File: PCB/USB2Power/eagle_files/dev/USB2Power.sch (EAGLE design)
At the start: 7 parts, among them SW1 PCM12SMTR

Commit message: All connected up. Also added ground for the other two header pins as opposed to NC. Made connections a little better. Some known DRC failures.
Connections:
- net GND: now also JP1.3, JP1.4
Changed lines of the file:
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@@
 <label x="73.66" y="22.86" size="1.778" layer="95"/>
+</segment>
+<segment>
+<pinref part="JP1" gate="G$1" pin="4"/>
+<wire x1="63.5" y1="33.02" x2="76.2" y2="33.02" width="0.1524" layer="91"/>
+<label x="71.12" y="33.02" size="1.778" layer="95"/>
+</segment>
+<segment>
+<pinref part="JP1" gate="G$1" pin="3"/>
+<wire x1="63.5" y1="30.48" x2="76.2" y2="30.48" width="0.1524" layer="91"/>
+<label x="71.12" y="30.48" size="1.778" layer="95"/>
 </segment>
 </net>

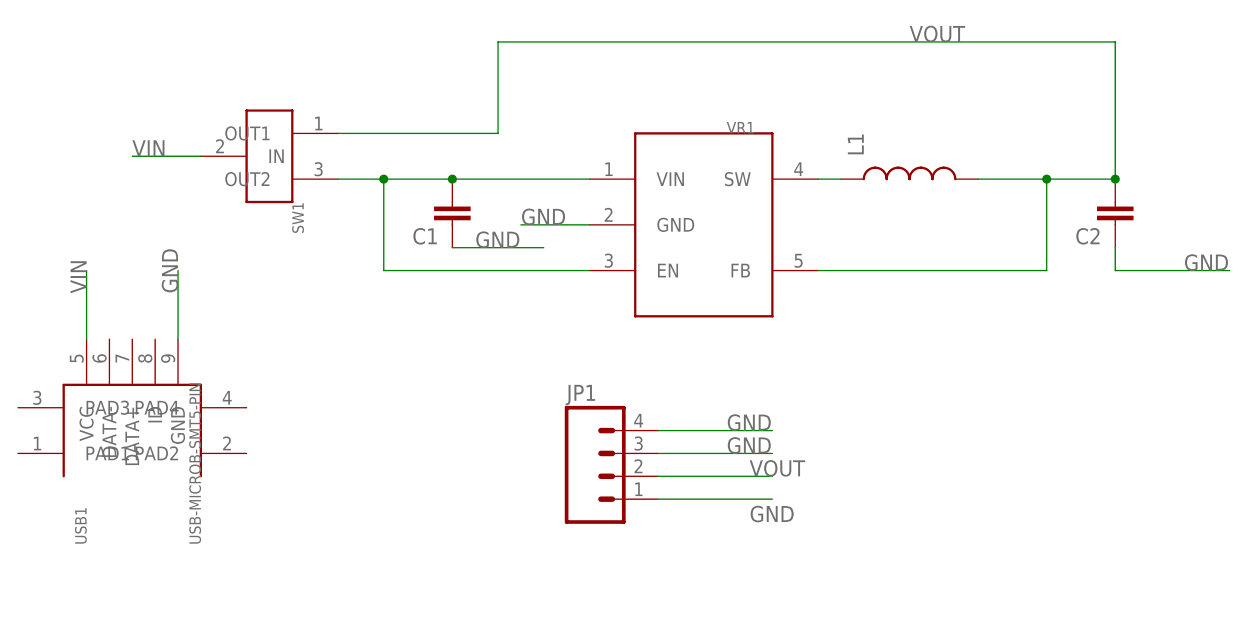
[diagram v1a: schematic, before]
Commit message: Add separate headers for 5V and 3V power outputs. Joint header + inductor may have been causing problems.
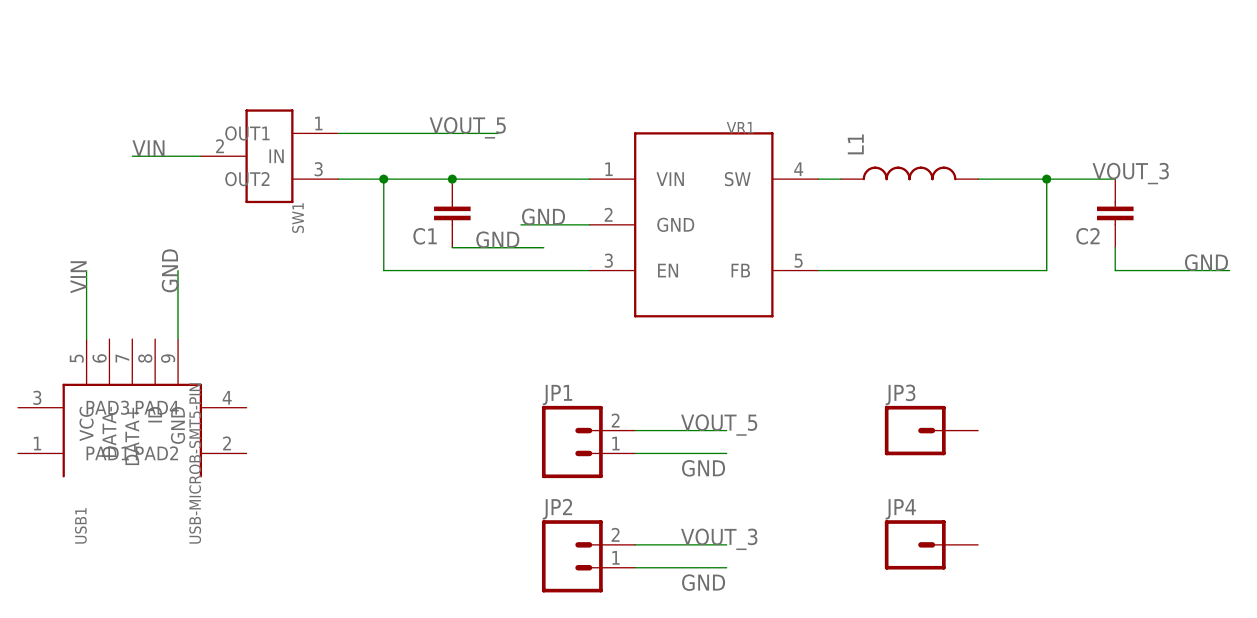
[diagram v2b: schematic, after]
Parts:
- added JP2: (no value), SparkFun-Connectors:M02PTH
- added JP3, JP4: (no value), SparkFun-Connectors:M01PTH
- JP1: device SparkFun-Connectors:M04PTH -> SparkFun-Connectors:M02PTH
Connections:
- removed net VOUT: C2.2, JP1.2, L1.2, SW1.OUT1, VR1.FB
- new net VOUT_3: C2.2, JP2.2, L1.2, VR1.FB
- new net VOUT_5: JP1.2, SW1.OUT1
- net GND: now also JP2.1; no longer JP1.3, JP1.4
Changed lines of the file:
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@@
 <part name="USB1" library="freddyLibr" deviceset="USB-MICROB-SMT" device="5-PIN"/>
 <part name="VR1" library="freddyLibr" deviceset="ADP2108" device=""/>
-<part name="JP1" library="SparkFun-Connectors" deviceset="M04" device="PTH"/>
+<part name="JP1" library="SparkFun-Connectors" deviceset="M02" device="PTH"/>
+<part name="JP2" library="SparkFun-Connectors" deviceset="M02" device="PTH"/>
+<part name="JP3" library="SparkFun-Connectors" deviceset="M01" device="PTH"/>
+<part name="JP4" library="SparkFun-Connectors" deviceset="M01" device="PTH"/>
 </parts>
 <sheets>
@@
 <instance part="USB1" gate="G$1" x="5.08" y="33.02" rot="R90"/>
 <instance part="VR1" gate="G$1" x="68.58" y="55.88"/>
-<instance part="JP1" gate="G$1" x="58.42" y="27.94"/>
+<instance part="JP1" gate="G$1" x="53.34" y="30.48"/>
+<instance part="JP2" gate="G$1" x="53.34" y="17.78"/>
+<instance part="JP3" gate="G$1" x="91.44" y="33.02"/>
+<instance part="JP4" gate="G$1" x="91.44" y="20.32"/>
 </instances>
 <busses>
@@
 </segment>
 <segment>
-<pinref part="JP1" gate="G$1" pin="1"/>
-<wire x1="63.5" y1="25.4" x2="76.2" y2="25.4" width="0.1524" layer="91"/>
-<label x="73.66" y="22.86" size="1.778" layer="95"/>
+<pinref part="JP2" gate="G$1" pin="1"/>
+<wire x1="60.96" y1="17.78" x2="71.12" y2="17.78" width="0.1524" layer="91"/>
+<label x="66.04" y="15.24" size="1.778" layer="95"/>
 </segment>
 <segment>
-<pinref part="JP1" gate="G$1" pin="4"/>
-<wire x1="63.5" y1="33.02" x2="76.2" y2="33.02" width="0.1524" layer="91"/>
-<label x="71.12" y="33.02" size="1.778" layer="95"/>
-</segment>
-<segment>
-<pinref part="JP1" gate="G$1" pin="3"/>
-<wire x1="63.5" y1="30.48" x2="76.2" y2="30.48" width="0.1524" layer="91"/>
-<label x="71.12" y="30.48" size="1.778" layer="95"/>
+<pinref part="JP1" gate="G$1" pin="1"/>
+<wire x1="60.96" y1="30.48" x2="71.12" y2="30.48" width="0.1524" layer="91"/>
+<label x="66.04" y="27.94" size="1.778" layer="95"/>
 </segment>
 </net>
@@
 </segment>
 </net>
-<net name="VOUT" class="0">
+<net name="VOUT_3" class="0">
 <segment>
+<pinref part="VR1" gate="G$1" pin="FB"/>
+<pinref part="C2" gate="G$1" pin="2"/>
 <pinref part="L1" gate="G$1" pin="2"/>
 <wire x1="99.06" y1="60.96" x2="106.68" y2="60.96" width="0.1524" layer="91"/>
+<junction x="106.68" y="60.96"/>
+<wire x1="106.68" y1="60.96" x2="114.3" y2="60.96" width="0.1524" layer="91"/>
 <wire x1="106.68" y1="60.96" x2="106.68" y2="50.8" width="0.1524" layer="91"/>
-<pinref part="VR1" gate="G$1" pin="FB"/>
 <wire x1="106.68" y1="50.8" x2="81.28" y2="50.8" width="0.1524" layer="91"/>
-<junction x="106.68" y="60.96"/>
-<pinref part="C2" gate="G$1" pin="2"/>
-<wire x1="106.68" y1="60.96" x2="114.3" y2="60.96" width="0.1524" layer="91"/>
-<junction x="114.3" y="60.96"/>
+<label x="111.76" y="60.96" size="1.778" layer="95"/>
+</segment>
+<segment>
+<pinref part="JP2" gate="G$1" pin="2"/>
+<wire x1="60.96" y1="20.32" x2="71.12" y2="20.32" width="0.1524" layer="91"/>
+<label x="66.04" y="20.32" size="1.778" layer="95"/>
+</segment>
+</net>
+<net name="VOUT_5" class="0">
+<segment>
 <pinref part="SW1" gate="G$1" pin="OUT1"/>
 <wire x1="27.94" y1="66.04" x2="45.72" y2="66.04" width="0.1524" layer="91"/>
-<wire x1="45.72" y1="66.04" x2="45.72" y2="76.2" width="0.1524" layer="91"/>
-<wire x1="45.72" y1="76.2" x2="114.3" y2="76.2" width="0.1524" layer="91"/>
-<wire x1="114.3" y1="76.2" x2="114.3" y2="60.96" width="0.1524" layer="91"/>
-<label x="91.44" y="76.2" size="1.778" layer="95"/>
+<label x="38.1" y="66.04" size="1.778" layer="95"/>
 </segment>
 <segment>
 <pinref part="JP1" gate="G$1" pin="2"/>
-<wire x1="63.5" y1="27.94" x2="76.2" y2="27.94" width="0.1524" layer="91"/>
-<label x="73.66" y="27.94" size="1.778" layer="95"/>
+<wire x1="60.96" y1="33.02" x2="71.12" y2="33.02" width="0.1524" layer="91"/>
+<label x="66.04" y="33.02" size="1.778" layer="95"/>
 </segment>
 </net>

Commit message: Finalize 2.0 version of board. Routed and labeled.
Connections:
- net GND: now also JP3.1, JP4.1
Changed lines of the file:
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@@
 <label x="66.04" y="27.94" size="1.778" layer="95"/>
+</segment>
+<segment>
+<pinref part="JP3" gate="G$1" pin="1"/>
+<wire x1="99.06" y1="33.02" x2="109.22" y2="33.02" width="0.1524" layer="91"/>
+<label x="104.14" y="33.02" size="1.778" layer="95"/>
+</segment>
+<segment>
+<pinref part="JP4" gate="G$1" pin="1"/>
+<wire x1="99.06" y1="20.32" x2="109.22" y2="20.32" width="0.1524" layer="91"/>
+<label x="104.14" y="20.32" size="1.778" layer="95"/>
 </segment>
 </net>
